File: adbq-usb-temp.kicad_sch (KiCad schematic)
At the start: 34 parts, among them J4 USB_C_Receptacle_USB2.0_14P, U1 ESP32-S3FH4R2, U7 USBLC6-2SC6, Y1 48M

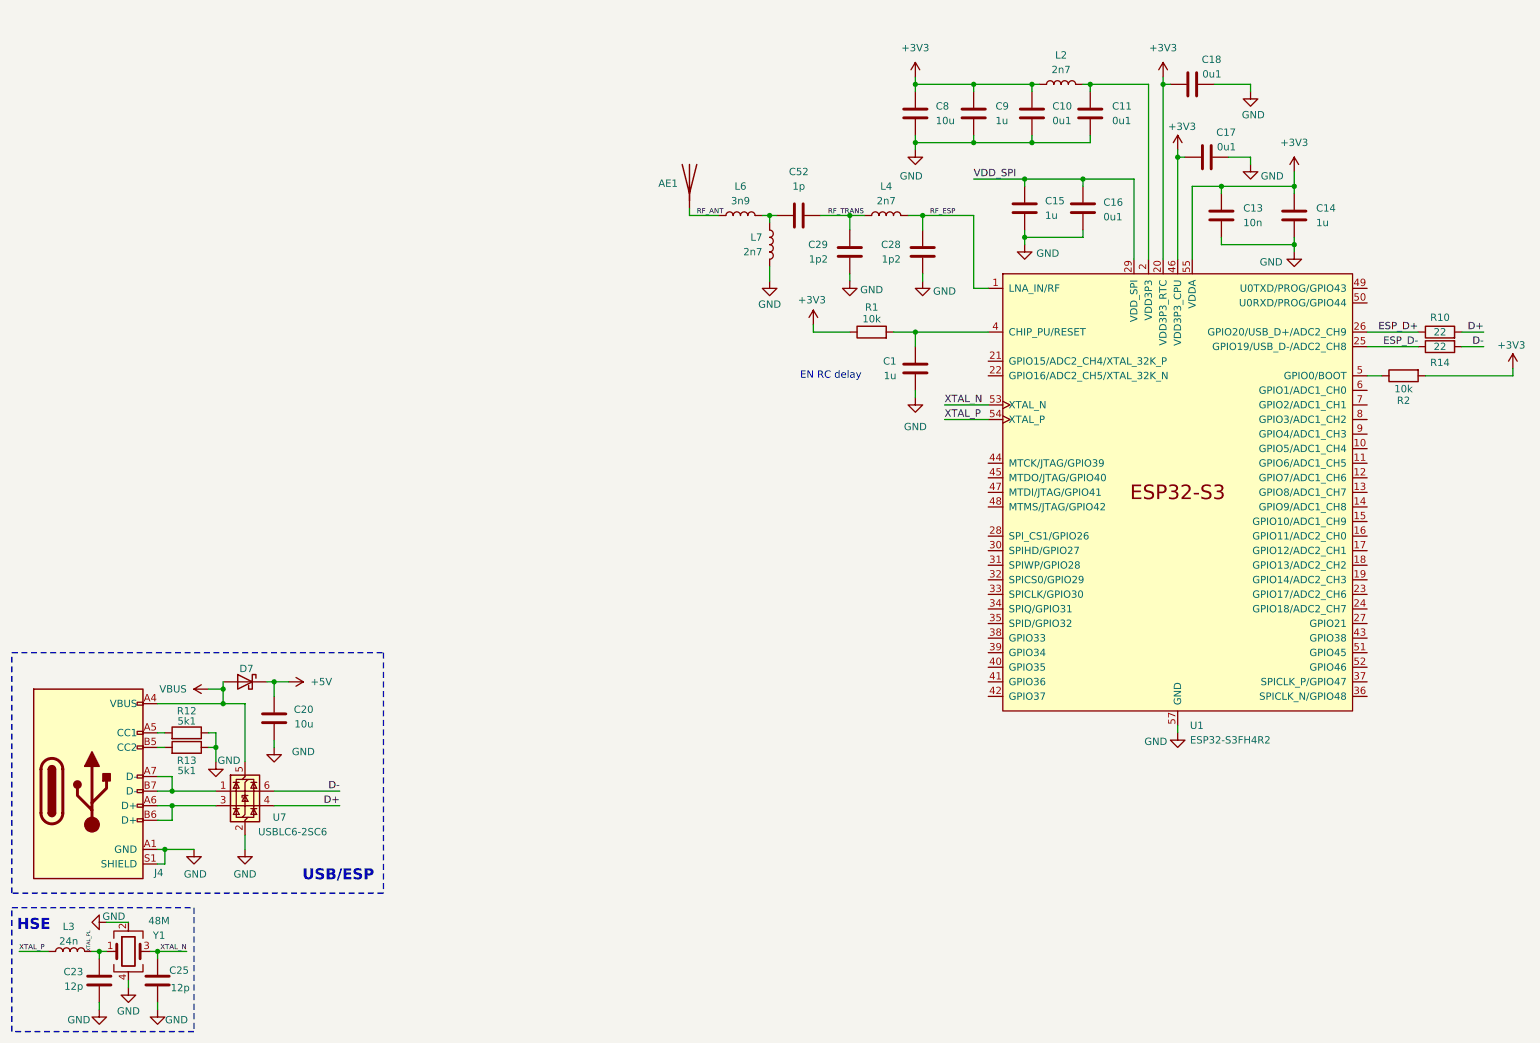
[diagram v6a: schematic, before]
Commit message: schem: add TMP117 temperature sensor
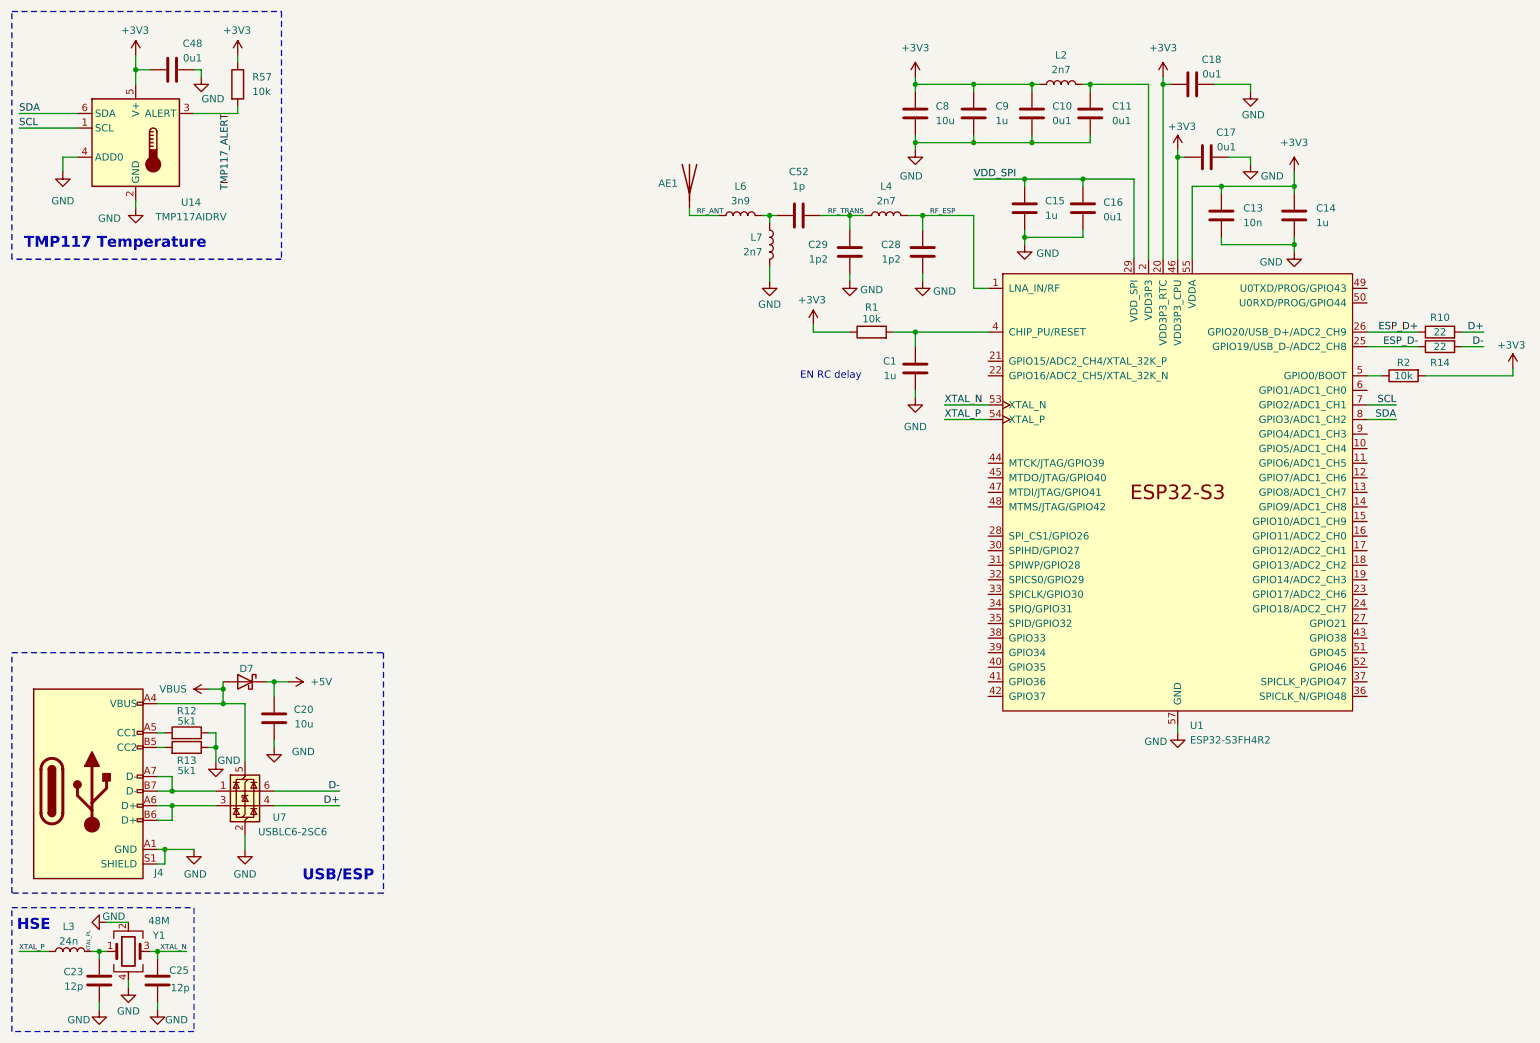
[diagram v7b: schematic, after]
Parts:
- added C48: 0u1, Capacitor_SMD:C_0402_1005Metric, symbol Device:C
- added R57: 10k, Resistor_SMD:R_0402_1005Metric, symbol Device:R
- added U14: TMP117AIDRV, Package_SON:WSON-6-1EP_2x2mm_P0.65mm_EP1x1.6mm, symbol Sensor_Temperature:TMP117xxDRV
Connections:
- net +3V3: now also C48.1, R57.1, U14.5 (V+)
- net GND: now also C48.2, U14.2 (GND), U14.4 (ADD0)
- net SCL: now reaches U1.7 (GPIO2/ADC1_CH1)
- net SCL: now also U14.1 (SCL)
- net SDA: now reaches U1.8 (GPIO3/ADC1_CH2)
- net SDA: now also U14.6 (SDA)
- new net TMP117_ALERT: R57.2, U14.3 (ALERT)
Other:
- note added: "TMP117 Temperature"

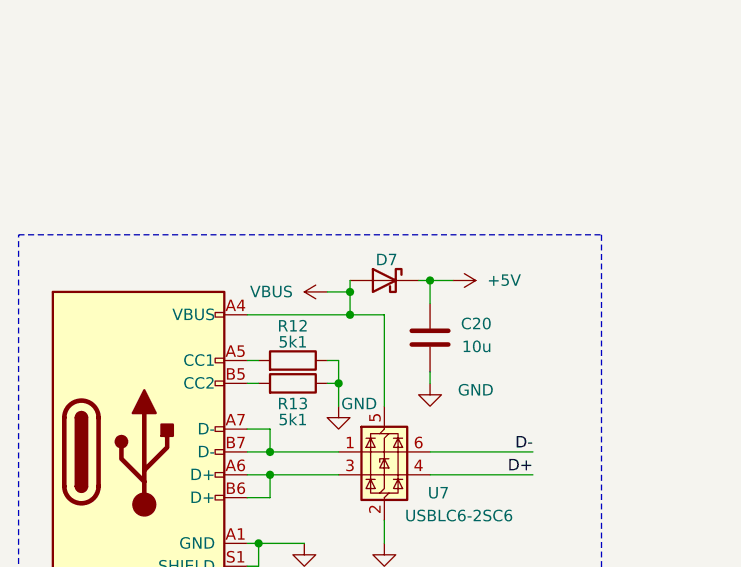
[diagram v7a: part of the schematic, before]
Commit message: POC(schem): remove USB-C diode
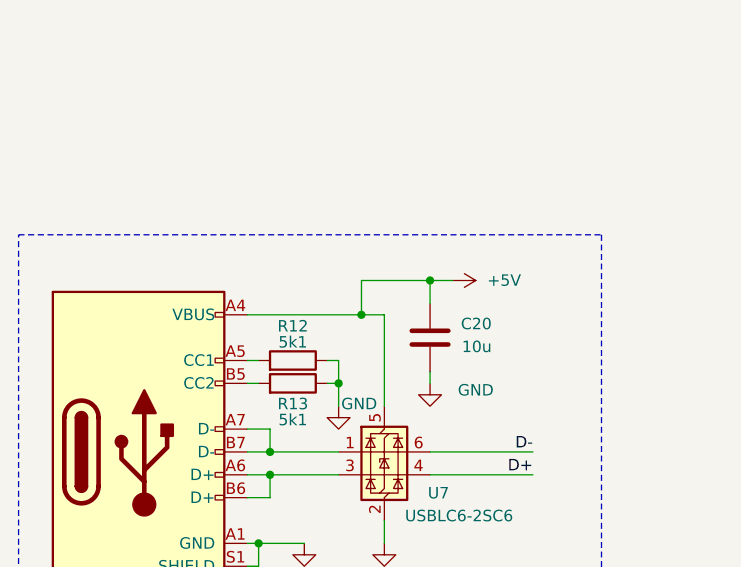
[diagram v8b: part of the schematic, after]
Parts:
- removed D7: D_Schottky, Diode_SMD:D_SMA, symbol Device:D_Schottky
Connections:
- net VBUS is gone; now on net +5V: J4.A4 (VBUS), J4.A9 (VBUS), J4.B4 (VBUS), J4.B9 (VBUS), U7.5 (VBUS)
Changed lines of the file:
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@@
 	)
 	(junction
-		(at 227.33 46.99)
+		(at 54.61 137.16)
 		(diameter 0)
 		(color 0 0 0 0)
 	)
 	(junction
-		(at 53.34 134.62)
+		(at 227.33 46.99)
 		(diameter 0)
 		(color 0 0 0 0)
@@
 	)
 	(junction
-		(at 53.34 137.16)
-		(diameter 0)
-		(color 0 0 0 0)
-	)
-	(junction
 		(at 173.99 39.37)
 		(diameter 0)
@@
 	(wire
 		(pts
-			(xy 53.34 134.62) (xy 50.8 134.62)
-		)
-		(stroke
-			(width 0)
-			(type default)
-		)
-	)
-	(wire
-		(pts
 			(xy 41.91 189.23) (xy 41.91 190.5)
 		)
@@
 	(wire
 		(pts
-			(xy 53.34 137.16) (xy 53.34 134.62)
-		)
-		(stroke
-			(width 0)
-			(type default)
-		)
-	)
-	(wire
-		(pts
 			(xy 203.2 55.88) (xy 193.04 55.88)
 		)
@@
 	(wire
 		(pts
+			(xy 54.61 133.35) (xy 54.61 137.16)
+		)
+		(stroke
+			(width 0)
+			(type default)
+		)
+	)
+	(wire
+		(pts
 			(xy 179.07 87.63) (xy 186.69 87.63)
 		)
@@
 	(wire
 		(pts
+			(xy 54.61 133.35) (xy 62.23 133.35)
+		)
+		(stroke
+			(width 0)
+			(type default)
+		)
+	)
+	(wire
+		(pts
 			(xy 204.47 29.21) (xy 204.47 30.48)
 		)
@@
 	(wire
 		(pts
-			(xy 53.34 137.16) (xy 41.91 137.16)
+			(xy 41.91 137.16) (xy 54.61 137.16)
 		)
 		(stroke
@@
 	(wire
 		(pts
-			(xy 53.34 134.62) (xy 53.34 133.35)
-		)
-		(stroke
-			(width 0)
-			(type default)
-		)
-	)
-	(wire
-		(pts
 			(xy 184.15 38.1) (xy 184.15 39.37)
 		)
@@
 	(wire
 		(pts
-			(xy 57.15 137.16) (xy 53.34 137.16)
-		)
-		(stroke
-			(width 0)
-			(type default)
-		)
-	)
-	(wire
-		(pts
 			(xy 219.71 59.69) (xy 219.71 41.91)
 		)
@@
 	(wire
 		(pts
+			(xy 54.61 137.16) (xy 57.15 137.16)
+		)
+		(stroke
+			(width 0)
+			(type default)
+		)
+	)
+	(wire
+		(pts
 			(xy 257.81 87.63) (xy 252.73 87.63)
 		)
@@
 	(wire
 		(pts
-			(xy 62.23 133.35) (xy 60.96 133.35)
-		)
-		(stroke
-			(width 0)
-			(type default)
-		)
-	)
-	(wire
-		(pts
 			(xy 41.91 180.34) (xy 46.99 180.34)
 		)
@@
 	)
 	(symbol
-		(lib_id "power:VBUS")
-		(at 50.8 134.62 90)
-		(mirror x)
-		(unit 1)
-		(exclude_from_sim no)
-		(in_bom yes)
-		(on_board yes)
-		(dnp no)
-		(fields_autoplaced yes)
-		(property "Reference" "#PWR051"
-			(at 54.61 134.62 0)
-			(effects
-				(font
-					(size 1.27 1.27)
-				)
-				(hide yes)
-			)
-		)
-		(property "Value" "VBUS"
-			(at 46.99 134.6199 90)
-			(effects
-				(font
-					(size 1.27 1.27)
-				)
-				(justify left)
-			)
-		)
-		(property "Footprint" ""
-			(at 50.8 134.62 0)
-			(effects
-				(font
-					(size 1.27 1.27)
-				)
-				(hide yes)
-			)
-		)
-		(property "Datasheet" ""
-			(at 50.8 134.62 0)
-			(effects
-				(font
-					(size 1.27 1.27)
-				)
-				(hide yes)
-			)
-		)
-		(property "Description" "Power symbol creates a global label with name \"VBUS\""
-			(at 50.8 134.62 0)
-			(effects
-				(font
-					(size 1.27 1.27)
-				)
-				(hide yes)
-			)
-		)
-		(pin "1"
-		)
-		(instances
-			(project "adbq-usb-temp"
-				(path "/683f6451-7bb7-4686-955a-dbaefe964302"
-					(reference "#PWR051")
-					(unit 1)
-				)
-			)
-		)
-	)
-	(symbol
 		(lib_id "power:+3V3")
 		(at 55.88 24.13 0)
@@
 					(unit 1)
 				)
-			)
-		)
-	)
-	(symbol
-		(lib_id "Device:D_Schottky")
-		(at 57.15 133.35 0)
-		(mirror y)
-		(unit 1)
-		(exclude_from_sim no)
-		(in_bom yes)
-		(on_board yes)
-		(dnp no)
-		(property "Reference" "D7"
-			(at 57.404 131.064 0)
-			(effects
-				(font
-					(size 1.27 1.27)
-				)
-			)
-		)
-		(property "Value" "D_Schottky"
-			(at 57.4675 129.54 0)
-			(effects
-				(font
-					(size 1.27 1.27)
-				)
-				(hide yes)
-			)
-		)
-		(property "Footprint" "Diode_SMD:D_SMA"
-			(at 57.15 133.35 0)
-			(effects
-				(font
-					(size 1.27 1.27)
-				)
-				(hide yes)
-			)
-		)
-		(property "Datasheet" "~"
-			(at 57.15 133.35 0)
-			(effects
-				(font
-					(size 1.27 1.27)
-				)
-				(hide yes)
-			)
-		)
-		(property "Description" "Schottky diode"
-			(at 57.15 133.35 0)
-			(effects
-				(font
-					(size 1.27 1.27)
-				)
-				(hide yes)
-			)
-		)
-		(property "Manufacturer" "Microdiode Semiconductor (MDD)"
-			(at 57.15 133.35 0)
-			(effects
-				(font
-					(size 1.27 1.27)
-				)
-				(hide yes)
-			)
-		)
-		(property "Manufacturer Part Number" "SS54"
-			(at 57.15 133.35 0)
-			(effects
-				(font
-					(size 1.27 1.27)
-				)
-				(hide yes)
-			)
-		)
-		(property "Basic" "Y"
-			(at 57.15 133.35 0)
-			(effects
-				(font
-					(size 1.27 1.27)
-				)
-				(hide yes)
-			)
-		)
-		(property "JLCPCB Part #" "C22452"
-			(at 57.15 133.35 0)
-			(effects
-				(font
-					(size 1.27 1.27)
-				)
-				(hide yes)
-			)
-		)
-		(pin "2"
-		)
-		(pin "1"
-		)
-		(instances
-			(project "adbq-usb-temp"
-				(path "/683f6451-7bb7-4686-955a-dbaefe964302"
-					(reference "D7")
-					(unit 1)
-				)
